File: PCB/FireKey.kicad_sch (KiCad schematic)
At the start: 74 parts, among them SW1 SW_MEC_4A, U1 Arduino_Pro_Micro_USB-C

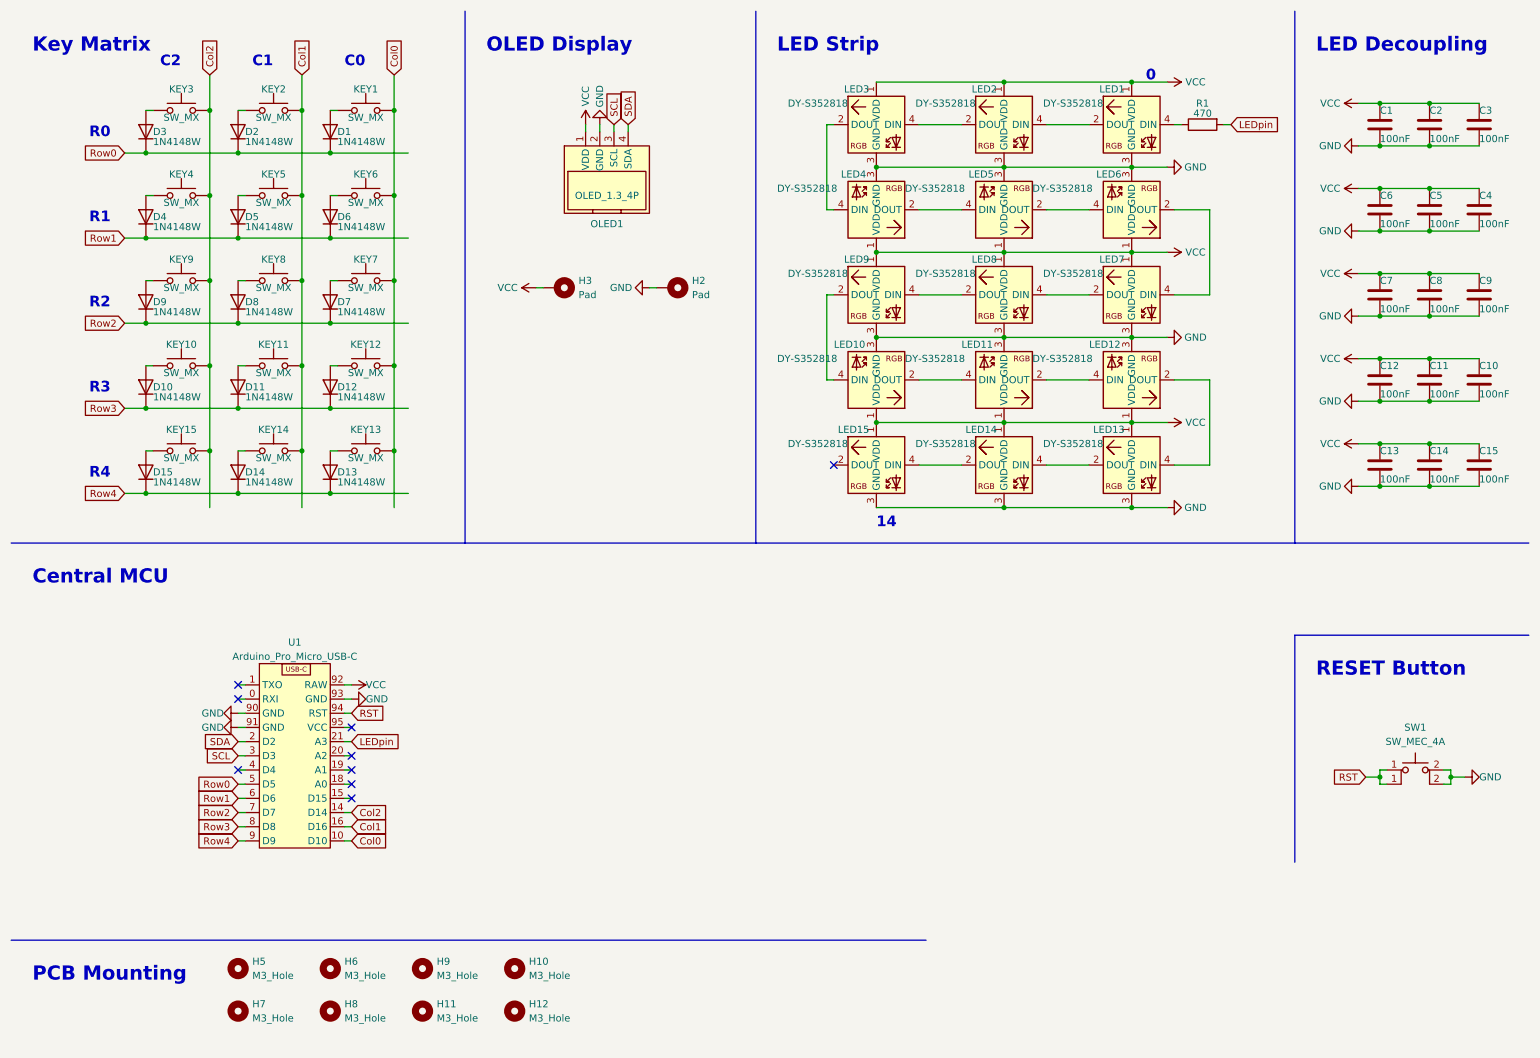
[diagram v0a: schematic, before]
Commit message: small changes to schematic; passed DRC
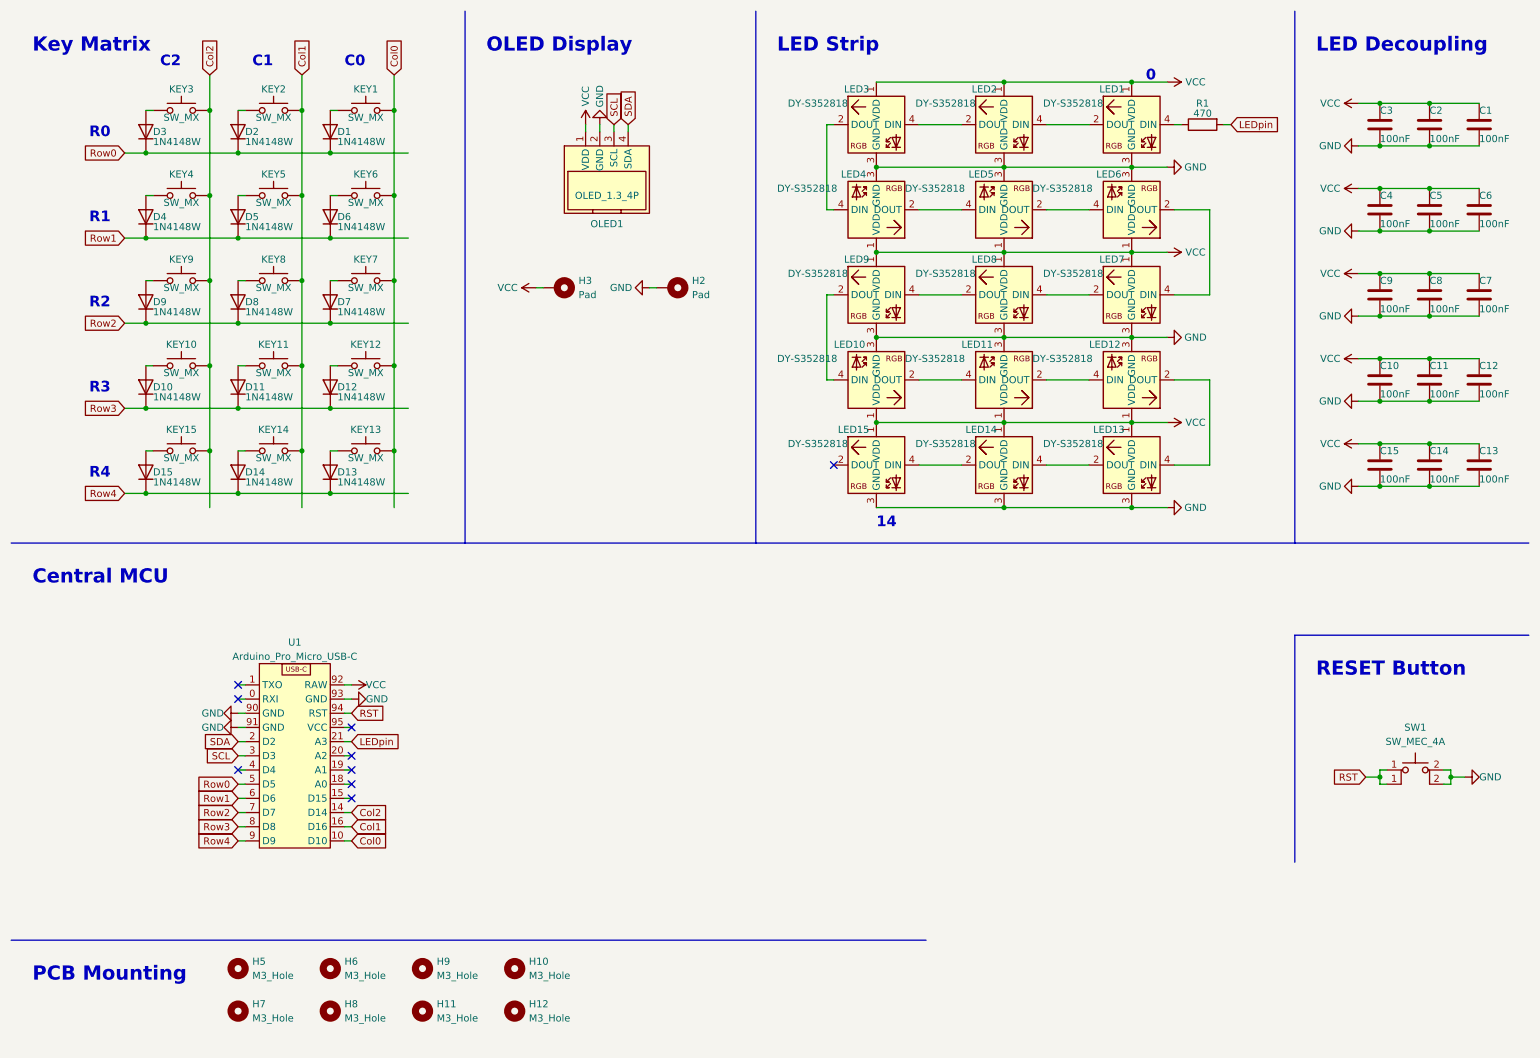
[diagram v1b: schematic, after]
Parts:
- KEY1, KEY10, KEY11, KEY12, KEY13, KEY14, KEY15, KEY2, KEY3, KEY4, KEY5, KEY6, KEY7, KEY8, KEY9: Part# (none) -> -
- renumbered C3 to C1, C12 to C10, C10 to C12, C15 to C13, C13 to C15, C1 to C3, C6 to C4, C4 to C6, C9 to C7, C7 to C9
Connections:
- net at D8.2 (A), KEY8.1 (A): no longer KEY8.2 (A)
- net at D10.2 (A), KEY10.1 (A): no longer KEY10.2 (A)
- net at D11.2 (A), KEY11.1 (A): no longer KEY11.2 (A)
- net at D12.2 (A), KEY12.1 (A): no longer KEY12.2 (A)
- net at D7.2 (A), KEY7.1 (A): no longer KEY7.2 (A)
- net at D9.2 (A), KEY9.1 (A): no longer KEY9.2 (A)
- net at D15.2 (A), KEY15.1 (A): no longer KEY15.2 (A)
- net at D2.2 (A), KEY2.1 (A): no longer KEY2.2 (A)
- net at D3.2 (A), KEY3.1 (A): no longer KEY3.2 (A)
- net at D14.2 (A), KEY14.1 (A): no longer KEY14.2 (A)
- net at D4.2 (A), KEY4.1 (A): no longer KEY4.2 (A)
- net at D5.2 (A), KEY5.1 (A): no longer KEY5.2 (A)
- net at D6.2 (A), KEY6.1 (A): no longer KEY6.2 (A)
- net at D13.2 (A), KEY13.1 (A): no longer KEY13.2 (A)
- net at D1.2 (A), KEY1.1 (A): no longer KEY1.2 (A)

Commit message: started working on V1.0.0
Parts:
- removed C10, C11, C12, C13, C14, C15: 100nF, Capacitor_SMD:C_0603_1608Metric_Pad1.08x0.95mm_HandSolder, symbol Device:C
- removed D10, D11, D12, D13, D14, D15: 1N4148W, Custom_Parts:D_SOD-123, symbol Device:D
- removed KEY10, KEY11, KEY12, KEY13, KEY14, KEY15: SW_MX, Button_Switch_Keyboard:SW_Cherry_MX_1.00u_PCB, symbol Custom_Parts:SW_MX_1u
- removed LED10, LED11, LED12, LED13, LED14, LED15: DY-S352818, Custom_Parts:DY-S352818-6812-2T, symbol Custom_Parts:DY-S352818/6812-2T
- added C? (x6): 100nF, Capacitor_SMD:C_0603_1608Metric_Pad1.08x0.95mm_HandSolder, symbol Device:C
- added D? (x6): 1N4148W, Custom_Parts:D_SOD-123, symbol Device:D
- added KEY? (x6): SW_MX, Button_Switch_Keyboard:SW_Cherry_MX_1.00u_PCB, symbol Custom_Parts:SW_MX_1u
- added LED? (x6): SK6812, Custom_Parts:DY-S352818-6812-2T, symbol Custom_Parts:DY-S352818/6812-2T
- added OLED?: OLED_1.3_4P, Custom_Module:OLED_1.3_4P_withM2.5Holes, symbol Custom_Modules:OLED_1.3_4P
- H?: renamed from H5; value M3_Hole -> M2.5_Hole; footprint MountingHole:MountingHole_3.2mm_M3 -> (none)
- H?: renamed from H6; value M3_Hole -> M2.5_Hole; footprint MountingHole:MountingHole_3.2mm_M3 -> (none)
- H?: renamed from H7; value M3_Hole -> M2.5_Hole; footprint MountingHole:MountingHole_3.2mm_M3 -> (none)
- H?: renamed from H9; value M3_Hole -> M2.5_Hole; footprint MountingHole:MountingHole_3.2mm_M3 -> (none)
- H?: renamed from H8; value M3_Hole -> M2.5_Hole; footprint MountingHole:MountingHole_3.2mm_M3 -> (none)
- H?: renamed from H11; value M3_Hole -> M2.5_Hole; footprint MountingHole:MountingHole_3.2mm_M3 -> (none)
- H?: renamed from H10; value M3_Hole -> M2.5_Hole; footprint MountingHole:MountingHole_3.2mm_M3 -> (none)
- H?: renamed from H12; value M3_Hole -> M2.5_Hole; footprint MountingHole:MountingHole_3.2mm_M3 -> (none)
- LED?: renamed from LED7; value DY-S352818 -> SK6812
- LED?: renamed from LED1; value DY-S352818 -> SK6812
- LED?: renamed from LED4; value DY-S352818 -> SK6812
- LED?: renamed from LED3; value DY-S352818 -> SK6812
- LED?: renamed from LED5; value DY-S352818 -> SK6812
- LED?: renamed from LED8; value DY-S352818 -> SK6812
- LED?: renamed from LED6; value DY-S352818 -> SK6812
- LED?: renamed from LED2; value DY-S352818 -> SK6812
- LED?: renamed from LED9; value DY-S352818 -> SK6812
- renumbered C3 to C?, C7 to C?, C5 to C?, C9 to C?, C1 to C?, C2 to C?, C4 to C?, C6 to C?, C8 to C?, D9 to D?, D7 to D?, D4 to D?, D1 to D?, D6 to D?, D8 to D?, D2 to D?, D5 to D?, D3 to D?, KEY8 to KEY?, KEY7 to KEY?, KEY2 to KEY?, KEY3 to KEY?, KEY9 to KEY?, KEY5 to KEY?, KEY4 to KEY?, KEY6 to KEY?, KEY1 to KEY?, OLED1 to OLED?, H3 to P?, H2 to P?, R1 to R?, SW1 to SW?, U1 to U?
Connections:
- net Col0: now also U?.5 (D5); no longer U?.10 (D10)
- net Col1: now also U?.6 (D6); no longer U?.16 (D16)
- net Col2: now also U?.7 (D7); no longer U?.14 (D14)
- net GND: now also C?.2, C?.2, C?.2, C?.2, C?.2, C?.2, LED?.3 (GND), LED?.3 (GND), LED?.3 (GND), LED?.3 (GND), LED?.3 (GND), LED?.3 (GND), OLED?.2 (GND)
- net LEDpin: no longer U?.21 (A3)
- net Row0: now also U?.10 (D10), D?.1 (K), D?.1 (K); no longer U?.5 (D5)
- net Row1: now also U?.16 (D16), D?.1 (K), D?.1 (K); no longer U?.6 (D6)
- net Row2: now also U?.14 (D14), D?.1 (K), D?.1 (K); no longer U?.7 (D7)
- net SCL: now also OLED?.3 (SCL)
- net SDA: now also OLED?.4 (SDA)
- net VCC: now also C?.1, C?.1, C?.1, C?.1, C?.1, C?.1, LED?.1 (VDD), LED?.1 (VDD), LED?.1 (VDD), LED?.1 (VDD), LED?.1 (VDD), LED?.1 (VDD), OLED?.1 (VDD)
- net at LED?.4 (DIN): now also LED?.2 (DOUT); no longer LED?.2 (DOUT)
- net at LED?.2 (DOUT): now also LED?.4 (DIN)
- net Row3 renamed Col3
- net Col3: now also KEY?.2 (B), KEY?.2 (B), KEY?.2 (B)
- net Row4 renamed Col4
- net Col4: now also KEY?.2 (B), KEY?.2 (B), KEY?.2 (B)
- new net: D?.2 (A), KEY?.1 (A) (x6)
- new net: LED?.2 (DOUT), LED?.4 (DIN) (x5)
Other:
- note added: "C3"
- note added: "C4"
- note added: "LED Strip Decoupling"
- note added: "OLED Displays"
- note added: "PCB Mounting Holes"
- note removed: "LED Decoupling"
- note removed: "OLED Display"
- note removed: "PCB Mounting"
- note removed: "R3"
- note removed: "R4"
- moved on the sheet: C?, D?, H?, KEY?, LED?, OLED?, P?, R?, SW?, U?

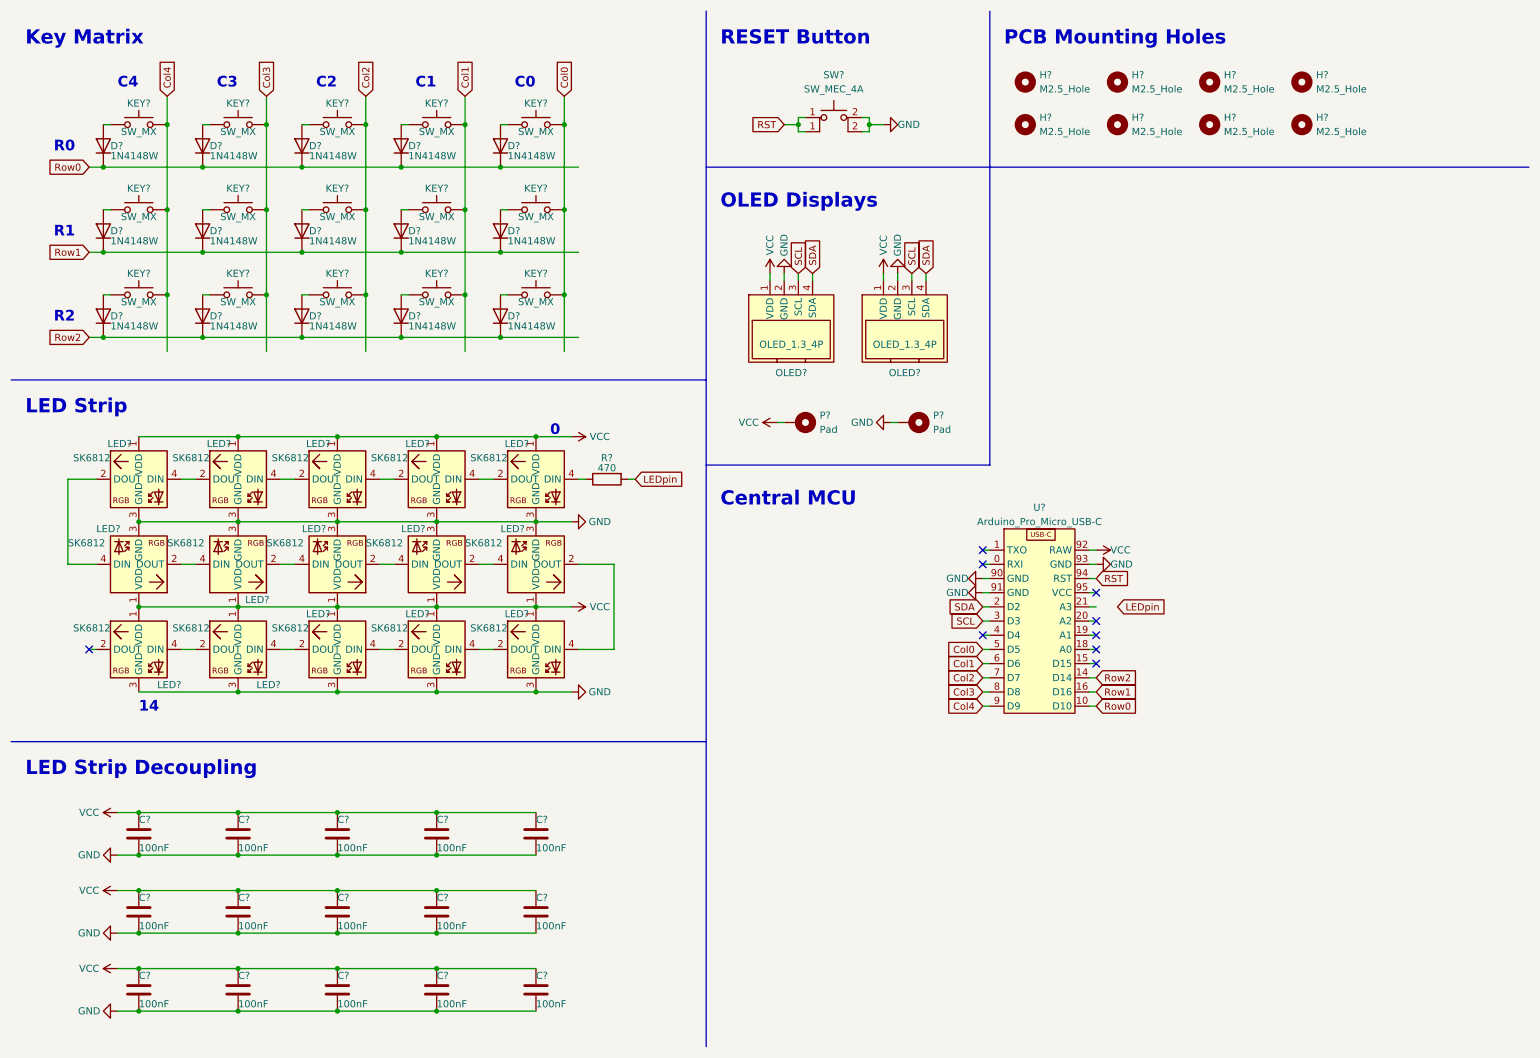
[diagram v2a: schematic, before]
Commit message: Worked on V1.0.0 Schematic
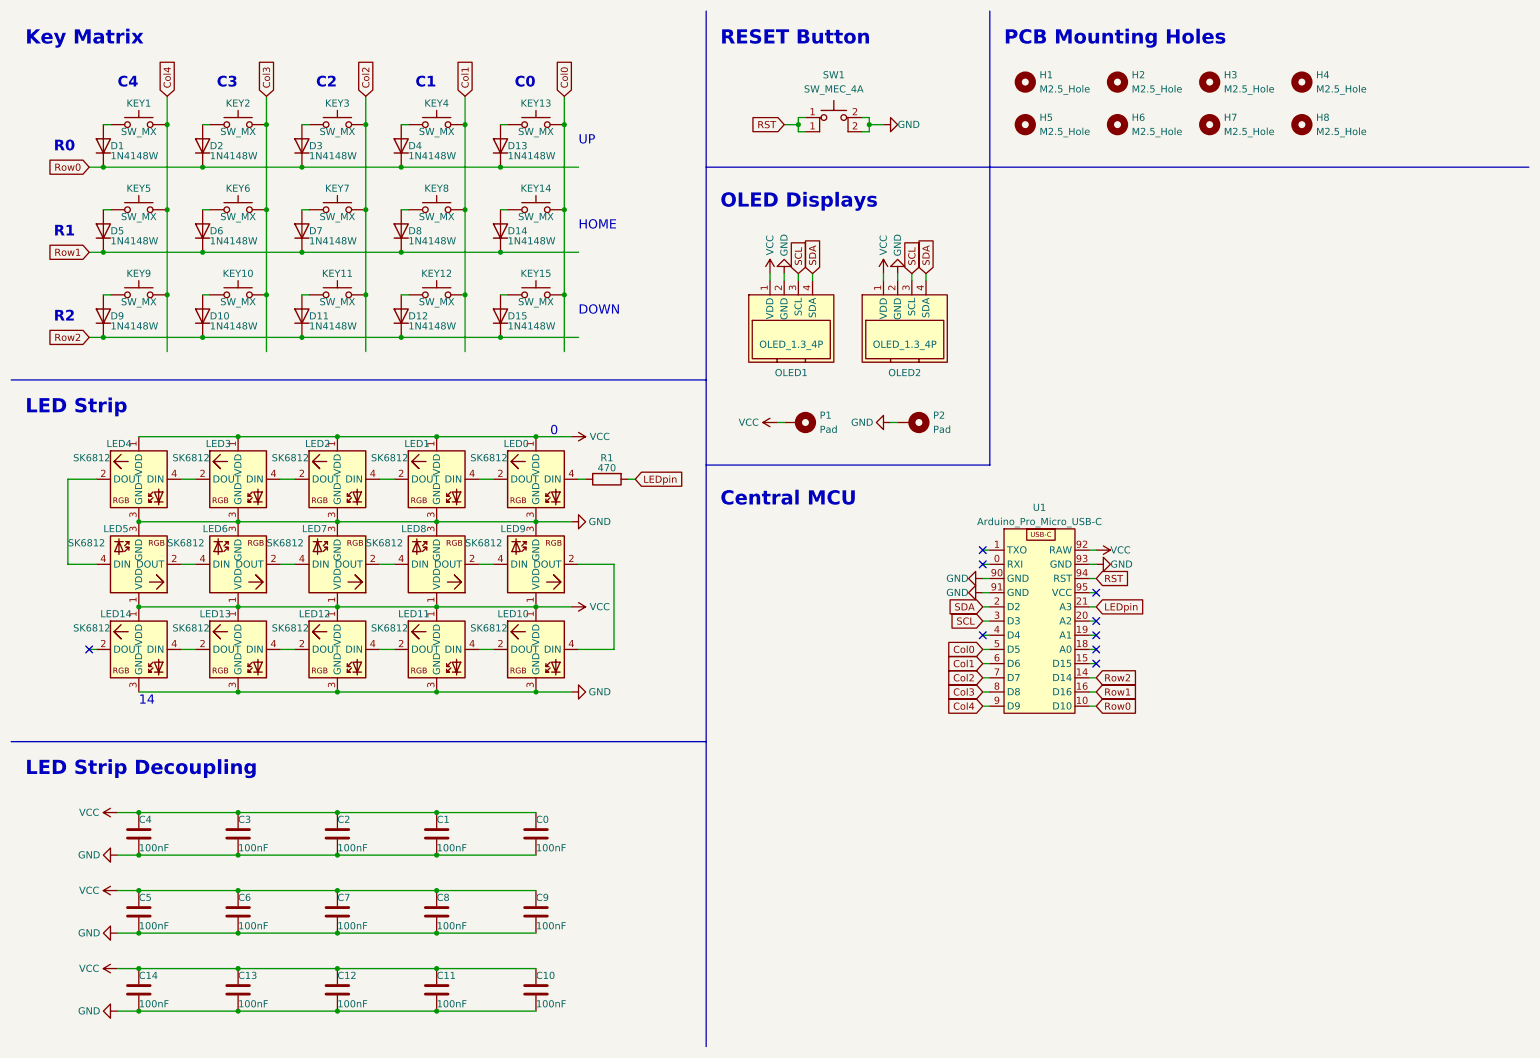
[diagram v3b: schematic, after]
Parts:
- H1, H2, H3, H4, H5, H6, H7, H8: renamed from H?; footprint (none) -> MountingHole:MountingHole_2.7mm_M2.5
- gave numbers to parts that had none: 67
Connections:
- net LEDpin: now also U1.21 (A3)
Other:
- note added: "DOWN"
- note added: "HOME"
- note added: "UP"

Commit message: Update FireKey.kicad_sch
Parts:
- removed SW1: SW_MEC_4A, Button_Switch_SMD:SW_SPST_TL3342, symbol Custom_Parts:SW_MEC_4A
- added Logo1: Logo_FireKey, Custom_FireKey:Logo_FireKey_32x9.4, symbol Custom_FireKey:Logo_FireKey
- added SW1: SW_MEC_4A, Button_Switch_SMD:SW_SPST_TL3342, symbol Custom_Parts:SW_MEC_4P
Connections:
- net GND: now also SW1.2
- net RST: now also SW1.1
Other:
- note added: "PCB Markings"
- moved on the sheet: U1
